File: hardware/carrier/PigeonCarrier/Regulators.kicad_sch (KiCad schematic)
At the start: 0 parts

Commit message: shortned readmes + start of power stuff
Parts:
- added C1: 100nF, PCM_JLCPCB:C_0402, symbol PCM_JLCPCB-Capacitors:0402,100nF,(2)
- added U2: LM74502DDFR, PigeonVision:Texas_DDF0008A_SOT-8_1.6x2.9mm_P0.65mm, symbol PigeonVision:LM74502DDFR
- added U3: INA226AIDGSR, PigeonVision:TI_DGS0010A_VSSOP-10_3x3mm_P0.5mm, symbol PigeonVision:INA226AIDGSR
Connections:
- new net VBAT_RAW: C1.1, U2.5 (VS)
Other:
- added sheet VBAT->5V_MAIN (batt_5V_main.kicad_sch)
- added sheet VBAT->5V_SDR (batt_5V_sdr.kicad_sch)
- note added: "Reverse Polarity Protection"
- note added: "UVLO:"

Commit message: carrier progress
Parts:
- added C2: 220nF, PCM_JLCPCB:C_0805, symbol PCM_JLCPCB-Capacitors:0805,220nF
- added C3: 100nF, PCM_JLCPCB:C_0402, symbol PCM_JLCPCB-Capacitors:0402,100nF,(2)
- added C8: 1uF, PCM_JLCPCB:C_0603, symbol PCM_JLCPCB-Capacitors:0603,1uF
- added C9: 220uF, JLCImport_Auto:EEEFK1V221P, symbol JLCImport_Auto:EEEFK1V221P
- added J4: PULL_PIN, symbol Connector_Generic:Conn_01x02
- added LED1, LED2, LED3: 0805G_Green, JLCImport_Auto:0805G_Green, symbol JLCImport_Auto:0805G_Green
- added Q1, Q2: CSD18540Q5B, Package_TO_SOT_SMD:TDSON-8-1, symbol Transistor_FET:CSD18540Q5B
- added R1: 7.5kΩ, PCM_JLCPCB:R_0402, symbol PCM_JLCPCB-Resistors:0402,7.5kΩ
- added R2, R20, R25: 1kΩ, PCM_JLCPCB:R_0402, symbol PCM_JLCPCB-Resistors:0402,1kΩ
- added R27: 560Ω, PCM_JLCPCB:R_0603, symbol PCM_JLCPCB-Resistors:0603,560Ω
- added R3: 51kΩ, PCM_JLCPCB:R_0402, symbol PCM_JLCPCB-Resistors:0402,51kΩ
- added R4: 4.7kΩ, PCM_JLCPCB:R_0402, symbol PCM_JLCPCB-Resistors:0402,4.7kΩ
- added R5, R7: 10, PCM_JLCPCB:R_0402, symbol Device:R
- added R6: 5mΩ, PigeonVision:Vishay_WSL2512_5mOhm_2W, symbol PigeonVision:WSL25125L000FEA18
- added TP1: VBAT_RAW, TestPoint:TestPoint_Pad_D2.0mm, symbol Connector:TestPoint
- added TP2: 5V_MAIN, TestPoint:TestPoint_Pad_D2.0mm, symbol Connector:TestPoint
- added TP3: 5V_RF, TestPoint:TestPoint_Pad_D2.0mm, symbol Connector:TestPoint
- added TP4: 4V_CAM, TestPoint:TestPoint_Pad_D2.0mm, symbol Connector:TestPoint
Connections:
- net VBAT_RAW: now also C2.1, Q1.5 (D), R1.1, R3.1, TP1.1
- net GND: now reaches U3.1 (A1)
- net GND: now also C1.2, U2.2 (GND), U3.2 (A0), U3.7 (GND), C3.2, C9.2, J4.2 (Pin_2), LED1.2 (K), LED2.2 (K), LED3.2 (K), R2.2, R4.2
- net at U3.10 (Vin+): now also C8.1, R5.2
- net SDA_0: now reaches U3.4 (SDA)
- net SCL_0: now reaches U3.5 (SCL)
- net +3V3: now reaches U3.6 (VS)
- net +3V3: now also C3.1
- net at U3.8 (Vbus): now also Q2.5 (D), R5.1, R6.1
- net at U3.9 (Vin-): now also C8.2, R7.2
- net PWR_EN: now reaches U2.1 (EN/UVLO)
- net PWR_EN: now also J4.1 (Pin_1), R1.2, R2.1
- net at U2.4 (VCAP): now also C2.2
- net at U2.6 (GATE): now also Q1.4 (G), Q2.4 (G)
- net at U2.7 (OV): now also R3.2, R4.1
- net at U2.8 (SRC): now also Q1.1 (S), Q1.2 (S), Q1.3 (S), Q2.1 (S), Q2.2 (S), Q2.3 (S)
- new net: LED2.1 (A), R25.2
- new net: LED1.1 (A), R20.2
- new net: LED3.1 (A), R27.2
- new net 4V_CAM: R27.1, TP4.1
- new net 5V_MAIN: R20.1, TP2.1
- new net 5V_RF: R25.1, TP3.1
- new net VBAT: C9.1, R6.2, R7.1
- no-connect marks 0 -> 2
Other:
- sheet VBAT->5V_SDR renamed VBAT->5V_RF
- added sheet 5V_MAIN -> Cam Regs (Camera_Regulators.kicad_sch)
- note added: "6 * 0.005 = 30mV"
- note added: "6^2 * 0.005 = 0.18W"
- note added: "ADDR: 1000000"
- note added: "Current Sensing"
- note added: "External switch: pin IN = closed / OFF Pin OUT = open / ON (UVLO still active) Connector / footprint TBD; no latching Shut down CM5 before reinserting pin"
- note added: "Fc = 8.0 kHz"
- note added: "Overvoltage: 14.81V"
- note added: "Pin Switch RBF Inhibit"
- note added: "Reverse Polarity, Overvoltage Protection"
- note added: "Shunt"
- note added: "UVLO: Off = 9.69V, Restart = 10.54V"
- note added: "~16.4A Measurement Limit"
- note added: "~2.1mA"
- note added: "~2.2mA"
- note removed: "Reverse Polarity Protection"
- note removed: "UVLO:"
- moved on the sheet: C1, U2, U3

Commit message: Update carrier schematics, parts library, and JLC rules
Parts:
- removed R27: 560Ω, PCM_JLCPCB:R_0603, symbol PCM_JLCPCB-Resistors:0603,560Ω
- removed R3: 51kΩ, PCM_JLCPCB:R_0402, symbol PCM_JLCPCB-Resistors:0402,51kΩ
- added R4: 56kΩ, PCM_JLCPCB:R_0402, symbol PCM_JLCPCB-Resistors:0402,56kΩ
- added R6: 220Ω, PCM_JLCPCB:R_0402, symbol PCM_JLCPCB-Resistors:0402,220Ω
- added TP4, TP5, TP6: GND, TestPoint:TestPoint_Pad_D2.0mm, symbol Connector:TestPoint
- TP2: renamed from TP4; value 4V_CAM -> 3V3_CAM
- renumbered C1 to C2, C2 to C3, C9 to C4, C8 to C5, C3 to C6, J4 to J6, LED3 to LED1, LED1 to LED2, LED2 to LED3, R7 to R10, R25 to R11, R1 to R2, R2 to R3, R4 to R5, R6 to R7, R20 to R8, R5 to R9, TP2 to TP3, TP3 to TP7, U2 to U1, U3 to U2
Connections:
- net GND: now also TP4.1, TP5.1, TP6.1
- net VBAT_RAW: now also R4.1
- net at R5.1, U1.7 (OV): now also R4.2
- net at LED1.1 (A): now also R6.2
- net +3V3 renamed 3V3_CM5
- net 4V_CAM renamed 3V3_CAM
- net 3V3_CAM: now also R6.1
- net SCL_0 renamed SENSOR_I2C_SCL
- net SDA_0 renamed SENSOR_I2C_SDA
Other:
- sheet 5V_MAIN -> Cam Regs renamed VBAT -> 3V3_CAM
- sheet VBAT -> 3V3_CAM ports: added none; removed 1V8_CAM_EN, 4V_CAM_EN
- sheet VBAT->5V_RF ports: added 5V_RF_EN; removed none
- note added: "External switch: pin IN = closed / OFF Pin OUT = open / ON"
- note added: "Overvoltage: 16.14V"
- note added: "To be placed near power TP for GND Springs"
- note removed: "External switch: pin IN = closed / OFF Pin OUT = open / ON (UVLO still active) Connector / footprint TBD; no latching Shut down CM5 before reinserting pin"
- note removed: "Overvoltage: 14.81V"
- note removed: "~2.1mA"
- moved on the sheet: LED1, LED2, LED3, R11, R8, TP2, TP3, TP7

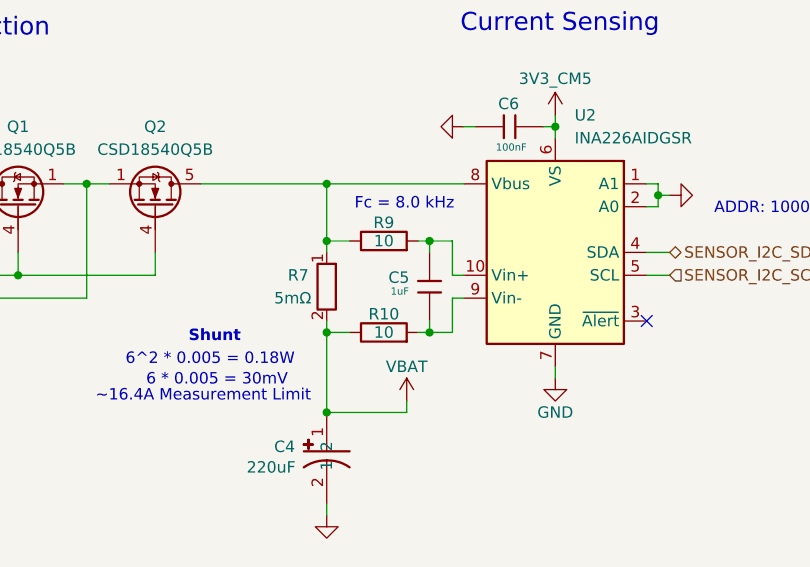
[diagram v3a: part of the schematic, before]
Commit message: Replace remaining 1 uF X5R capacitors with X7R
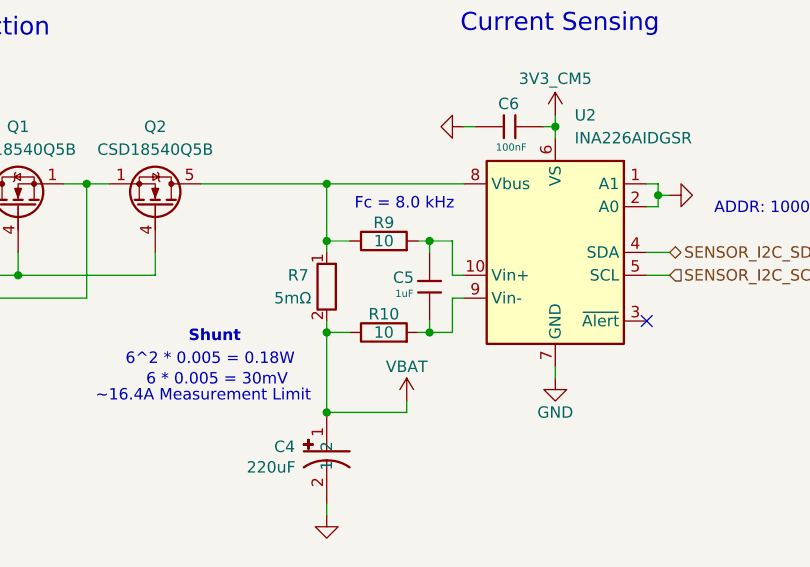
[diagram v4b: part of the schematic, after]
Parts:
- removed C5: 1uF, PCM_JLCPCB:C_0603, symbol PCM_JLCPCB-Capacitors:0603,1uF
- added C5: 1uF, PCM_JLCPCB:C_0805, symbol PCM_JLCPCB-Capacitors:0805,1uF
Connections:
- net at R9.2, U2.10 (Vin+): now also C5.1
- net at R10.2, U2.9 (Vin-): now also C5.2
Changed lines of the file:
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@@
+	)
+	(symbol
+		(lib_id "PCM_JLCPCB-Capacitors:0805,1uF")
+		(at 144.78 50.8 0)
+		(unit 1)
+		(body_style 1)
+		(exclude_from_sim no)
+		(in_bom yes)
+		(on_board yes)
+		(in_pos_files yes)
+		(dnp no)
+		(property "Reference" "C5"
+			(at 140.716 49.784 0)
+			(show_name no)
+			(do_not_autoplace no)
+			(effects
+				(font
+					(size 1.27 1.27)
+				)
+				(justify left)
+			)
+		)
+		(property "Value" "1uF"
+			(at 140.97 51.562 0)
+			(show_name no)
+			(do_not_autoplace no)
+			(effects
+				(font
+					(size 0.8 0.8)
+				)
+				(justify left)
+			)
+		)
+		(property "Footprint" "PCM_JLCPCB:C_0805"
+			(at 143.002 50.8 90)
+			(hide yes)
+			(show_name no)
+			(do_not_autoplace no)
+			(effects
+				(font
+					(size 1.27 1.27)
+				)
+			)
+		)
+		(property "Datasheet" "https://www.lcsc.com/datasheet/lcsc_datasheet_2304140030_Samsung-Electro-Mechanics-CL21B105KBFNNNE_C28323.pdf"
+			(at 144.78 50.8 0)
+			(hide yes)
+			(show_name no)
+			(do_not_autoplace no)
+			(effects
+				(font
+					(size 1.27 1.27)
+				)
+			)
+		)
+		(property "Description" "50V 1uF X7R ±10% 0805 Multilayer Ceramic Capacitors MLCC - SMD/SMT ROHS"
+			(at 144.78 50.8 0)
+			(hide yes)
+			(show_name no)
+			(do_not_autoplace no)
+			(effects
+				(font
+					(size 1.27 1.27)
+				)
+			)
+		)
+		(property "LCSC" "C28323"
+			(at 144.78 50.8 0)
+			(hide yes)
+			(show_name no)
+			(do_not_autoplace no)
+			(effects
+				(font
+					(size 1.27 1.27)
+				)
+			)
+		)
+		(property "Stock" "4334256"
+			(at 144.78 50.8 0)
+			(hide yes)
+			(show_name no)
+			(do_not_autoplace no)
+			(effects
+				(font
+					(size 1.27 1.27)
+				)
+			)
+		)
+		(property "Price" "0.012USD"
+			(at 144.78 50.8 0)
+			(hide yes)
+			(show_name no)
+			(do_not_autoplace no)
+			(effects
+				(font
+					(size 1.27 1.27)
+				)
+			)
+		)
+		(property "Process" "SMT"
+			(at 144.78 50.8 0)
+			(hide yes)
+			(show_name no)
+			(do_not_autoplace no)
+			(effects
+				(font
+					(size 1.27 1.27)
+				)
+			)
+		)
+		(property "Minimum Qty" "20"
+			(at 144.78 50.8 0)
+			(hide yes)
+			(show_name no)
+			(do_not_autoplace no)
+			(effects
+				(font
+					(size 1.27 1.27)
+				)
+			)
+		)
+		(property "Attrition Qty" "10"
+			(at 144.78 50.8 0)
+			(hide yes)
+			(show_name no)
+			(do_not_autoplace no)
+			(effects
+				(font
+					(size 1.27 1.27)
+				)
+			)
+		)
+		(property "Class" "Basic Component"
+			(at 144.78 50.8 0)
+			(hide yes)
+			(show_name no)
+			(do_not_autoplace no)
+			(effects
+				(font
+					(size 1.27 1.27)
+				)
+			)
+		)
+		(property "Category" "Capacitors,Multilayer Ceramic Capacitors MLCC - SMD/SMT"
+			(at 144.78 50.8 0)
+			(hide yes)
+			(show_name no)
+			(do_not_autoplace no)
+			(effects
+				(font
+					(size 1.27 1.27)
+				)
+			)
+		)
+		(property "Manufacturer" "Samsung Electro-Mechanics"
+			(at 144.78 50.8 0)
+			(hide yes)
+			(show_name no)
+			(do_not_autoplace no)
+			(effects
+				(font
+					(size 1.27 1.27)
+				)
+			)
+		)
+		(property "Part" "CL21B105KBFNNNE"
+			(at 144.78 50.8 0)
+			(hide yes)
+			(show_name no)
+			(do_not_autoplace no)
+			(effects
+				(font
+					(size 1.27 1.27)
+				)
+			)
+		)
+		(property "Voltage Rated" "50V"
+			(at 147.32 53.34 0)
+			(hide yes)
+			(show_name no)
+			(do_not_autoplace no)
+			(effects
+				(font
+					(size 0.8 0.8)
+				)
+				(justify left)
+			)
+		)
+		(property "Tolerance" "±10%"
+			(at 144.78 50.8 0)
+			(hide yes)
+			(show_name no)
+			(do_not_autoplace no)
+			(effects
+				(font
+					(size 1.27 1.27)
+				)
+			)
+		)
+		(property "Capacitance" "1uF"
+			(at 144.78 50.8 0)
+			(hide yes)
+			(show_name no)
+			(do_not_autoplace no)
+			(effects
+				(font
+					(size 1.27 1.27)
+				)
+			)
+		)
+		(property "Temperature Coefficient" "X7R"
+			(at 144.78 50.8 0)
+			(hide yes)
+			(show_name no)
+			(do_not_autoplace no)
+			(effects
+				(font
+					(size 1.27 1.27)
+				)
+			)
+		)
+		(pin "1"
+		)
+		(pin "2"
+		)
+		(instances
+			(project "PigeonCarrier"
+				(path "/6c8da0f4-34cf-43b9-a25b-857048b8016b/7986dfff-dfed-4d72-b8d7-0f8819bc467b"
+					(reference "C5")
+					(unit 1)
+				)
+			)
+		)
 	)
 	(symbol
@@
 					(unit 1)
 				)
-			)
-		)
-	)
-	(symbol
-		(lib_id "PCM_JLCPCB-Capacitors:0603,1uF")
-		(at 144.78 50.8 0)
-		(unit 1)
-		(body_style 1)
-		(exclude_from_sim no)
-		(in_bom yes)
-		(on_board yes)
-		(in_pos_files yes)
-		(dnp no)
-		(property "Reference" "C5"
-			(at 140.208 49.784 0)
-			(show_name no)
-			(do_not_autoplace no)
-			(effects
-				(font
-					(size 1.27 1.27)
-				)
-				(justify left)
-			)
-		)
-		(property "Value" "1uF"
-			(at 140.462 51.308 0)
-			(show_name no)
-			(do_not_autoplace no)
-			(effects
-				(font
-					(size 0.8 0.8)
-				)
-				(justify left)
-			)
-		)
-		(property "Footprint" "PCM_JLCPCB:C_0603"
-			(at 143.002 50.8 90)
-			(hide yes)
-			(show_name no)
-			(do_not_autoplace no)
-			(effects
-				(font
-					(size 1.27 1.27)
-				)
-			)
-		)
-		(property "Datasheet" "https://www.lcsc.com/datasheet/lcsc_datasheet_2304140030_Samsung-Electro-Mechanics-CL10A105KB8NNNC_C15849.pdf"
-			(at 144.78 50.8 0)
-			(hide yes)
-			(show_name no)
-			(do_not_autoplace no)
-			(effects
-				(font
-					(size 1.27 1.27)
-				)
-			)
-		)
-		(property "Description" "50V 1uF X5R ±10% 0603 Multilayer Ceramic Capacitors MLCC - SMD/SMT ROHS"
-			(at 144.78 50.8 0)
-			(hide yes)
-			(show_name no)
-			(do_not_autoplace no)
-			(effects
-				(font
-					(size 1.27 1.27)
-				)
-			)
-		)
-		(property "LCSC" "C15849"
-			(at 144.78 50.8 0)
-			(hide yes)
-			(show_name no)
-			(do_not_autoplace no)
-			(effects
-				(font
-					(size 1.27 1.27)
-				)
-			)
-		)
-		(property "Stock" "11535980"
-			(at 144.78 50.8 0)
-			(hide yes)
-			(show_name no)
-			(do_not_autoplace no)
-			(effects
-				(font
-					(size 1.27 1.27)
-				)
-			)
-		)
-		(property "Price" "0.008USD"
-			(at 144.78 50.8 0)
-			(hide yes)
-			(show_name no)
-			(do_not_autoplace no)
-			(effects
-				(font
-					(size 1.27 1.27)
-				)
-			)
-		)
-		(property "Process" "SMT"
-			(at 144.78 50.8 0)
-			(hide yes)
-			(show_name no)
-			(do_not_autoplace no)
-			(effects
-				(font
-					(size 1.27 1.27)
-				)
-			)
-		)
-		(property "Minimum Qty" "20"
-			(at 144.78 50.8 0)
-			(hide yes)
-			(show_name no)
-			(do_not_autoplace no)
-			(effects
-				(font
-					(size 1.27 1.27)
-				)
-			)
-		)
-		(property "Attrition Qty" "10"
-			(at 144.78 50.8 0)
-			(hide yes)
-			(show_name no)
-			(do_not_autoplace no)
-			(effects
-				(font
-					(size 1.27 1.27)
-				)
-			)
-		)
-		(property "Class" "Basic Component"
-			(at 144.78 50.8 0)
-			(hide yes)
-			(show_name no)
-			(do_not_autoplace no)
-			(effects
-				(font
-					(size 1.27 1.27)
-				)
-			)
-		)
-		(property "Category" "Capacitors,Multilayer Ceramic Capacitors MLCC - SMD/SMT"
-			(at 144.78 50.8 0)
-			(hide yes)
-			(show_name no)
-			(do_not_autoplace no)
-			(effects
-				(font
-					(size 1.27 1.27)
-				)
-			)
-		)
-		(property "Manufacturer" "Samsung Electro-Mechanics"
-			(at 144.78 50.8 0)
-			(hide yes)
-			(show_name no)
-			(do_not_autoplace no)
-			(effects
-				(font
-					(size 1.27 1.27)
-				)
-			)
-		)
-		(property "Part" "CL10A105KB8NNNC"
-			(at 144.78 50.8 0)
-			(hide yes)
-			(show_name no)
-			(do_not_autoplace no)
-			(effects
-				(font
-					(size 1.27 1.27)
-				)
-			)
-		)
-		(property "Voltage Rated" "50V"
-			(at 147.32 53.34 0)
-			(hide yes)
-			(show_name no)
-			(do_not_autoplace no)
-			(effects
-				(font
-					(size 0.8 0.8)
-				)
-				(justify left)
-			)
-		)
-		(property "Tolerance" "±10%"
-			(at 144.78 50.8 0)
-			(hide yes)
-			(show_name no)
-			(do_not_autoplace no)
-			(effects
-				(font
-					(size 1.27 1.27)
-				)
-			)
-		)
-		(property "Capacitance" "1uF"
-			(at 144.78 50.8 0)
-			(hide yes)
-			(show_name no)
-			(do_not_autoplace no)
-			(effects
-				(font
-					(size 1.27 1.27)
-				)
-			)
-		)
-		(property "Temperature Coefficient" "X5R"
-			(at 144.78 50.8 0)
-			(hide yes)
-			(show_name no)
-			(do_not_autoplace no)
-			(effects
-				(font
-					(size 1.27 1.27)
-				)
-			)
-		)
-		(pin "2"
-		)
-		(pin "1"
-		)
-		(instances
-			(project "PigeonCarrier"
-				(path "/6c8da0f4-34cf-43b9-a25b-857048b8016b/7986dfff-dfed-4d72-b8d7-0f8819bc467b"
-					(reference "C5")
-					(unit 1)
-				)

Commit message: finished rough layout
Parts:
- C2, C6: MPN (none) -> CL05B104KB54PNC
- C3: MPN (none) -> CL21B224KBFNNNE
- C4: footprint JLCImport_Auto:EEEFK1V221P -> PigeonVision:Panasonic_EEE-FK1V221P_CaseF_8x10.2mm; MPN (none) -> EEEFK1V221P
- C5: MPN (none) -> CL21B105KBFNNNE
- J6: footprint (none) -> Connector_AMASS:AMASS_XT30PW-M_1x02_P2.50mm_Horizontal; MPN (none) -> XT30PW-M; Manufacturer (none) -> AMASS
- LED1, LED2, LED3: MPN (none) -> KT-0805G
- Q1, Q2: footprint Package_TO_SOT_SMD:TDSON-8-1 -> PigeonVision:TI_CSD18540Q5B_Q5B; MPN (none) -> CSD18540Q5B; Manufacturer (none) -> Texas Instruments
- R10, R9: value 10 -> 10Ω; symbol Device:R -> PCM_JLCPCB-Resistors:0402,10Ω; Attrition Qty (none) -> 10; Category (none) -> Resistors,Chip Resistor - Surface Mount; Class (none) -> Basic Component; MPN (none) -> 0402WGF100JTCE; Minimum Qty (none) -> 20; Operating Temperature Range (none) -> -55°C~+155°C; Overload Voltage (Max) (none) -> 50V; Part (none) -> 0402WGF100JTCE; Power(Watts) (none) -> 62.5mW; Price (none) -> 0.004USD; Process (none) -> SMT; Resistance (none) -> 10Ω; Stock (none) -> 4873481; Temperature Coefficient (none) -> ±200ppm/°C; Tolerance (none) -> ±1%; Type (none) -> Thick Film Resistors
- R11, R3, R8: MPN (none) -> 0402WGF1001TCE
- R2: MPN (none) -> 0402WGF7501TCE
- R4: MPN (none) -> 0402WGF5602TCE
- R5: MPN (none) -> 0402WGF4701TCE
- R6: MPN (none) -> 0402WGF2200TCE
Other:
- note added: "Pin IN: closed / OFF Pin OUT: open / ON"
- note added: "Pin Switch"
- note removed: "External switch: pin IN = closed / OFF Pin OUT = open / ON"
- note removed: "Pin Switch RBF Inhibit"
- moved on the sheet: J6

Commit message: Update carrier placement and vertical connector libraries
Save the latest component placements and mechanical mounting changes. Include the vertical XT60/XT30 and camera connector symbols, footprints, redistributable CAD, licenses and documentation. Keep local-only vendor models ignored.

Validation: ERC has zero findings. Native KiCad loading and netlist comparison confirm all 152 schematic components and 681 numbered pads agree. Full DRC could not complete because the KiCad CLI aborted in this environment.
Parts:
- J6: footprint Connector_AMASS:AMASS_XT30PW-M_1x02_P2.50mm_Horizontal -> PigeonVision:AMASS_XT30UPB-M_1x02_P5.00mm_Vertical_2025; symbol Connector_Generic:Conn_01x02 -> PigeonVision:AMASS_XT30UPB_M_G_Y; JLC Part # (none) -> C428721; LCSC Part # (none) -> C428721; MPN XT30PW-M -> XT30UPB-M.G.Y; Sourcing note (none) -> JLC short MPN XT30UPB-M C428721;manufacturer2025V1 full yel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
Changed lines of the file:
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@@
 	)
 	(symbol
-		(lib_id "Connector_Generic:Conn_01x02")
+		(lib_id "PigeonVision:AMASS_XT30UPB_M_G_Y")
 		(at 44.45 88.9 0)
 		(mirror y)
@@
 			)
 		)
-		(property "Footprint" "Connector_AMASS:AMASS_XT30PW-M_1x02_P2.50mm_Horizontal"
+		(property "Footprint" "PigeonVision:AMASS_XT30UPB-M_1x02_P5.00mm_Vertical_2025"
 			(at 44.45 88.9 0)
 			(hide yes)
@@
 			)
 		)
-		(property "Datasheet" "https://www.tme.eu/Document/6eb2005a51a52592b3f19e8a450c54c8/XT30PW-M.pdf"
+		(property "Datasheet" "https://www.china-amass.net/uploads/XT30UPB-FM.rar"
 			(at 44.45 88.9 0)
 			(hide yes)
@@
 			)
 		)
-		(property "Description" "External COM-NO contact: pin inserted/lever pressed = closed/OFF; pin removed/lever released = open/ON. J6.1 directly inhibits EN/UVLO, J6.2 is GND."
+		(property "Description" "External COM-NO contact: pin inserted/lever pressed = closed/OFF; pin removed/lever released = open/ON. J6.1 directly inhibits EN/UVLO, J6.2 is GND. Vertical AMASS XT30UPB-M.G.Y; pin 1 keyed/minus-marked, pin 2 flat/plus-marked."
 			(at 44.45 88.9 0)
 			(hide yes)
@@
 			)
 		)
-		(property "MPN" "XT30PW-M"
+		(property "MPN" "XT30UPB-M.G.Y"
 			(at 36.83 87.63 0)
 			(hide yes)
@@
 			)
 		)
-	)
+	(property "LCSC Part #" "C428721" (at 44.45 88.9 0) (hide yes) (effects (font (size 1.27 1.27))))
+	(property "JLC Part #" "C428721" (at 44.45 88.9 0) (hide yes) (effects (font (size 1.27 1.27))))
+	(property "Sourcing note" "JLC short MPN XT30UPB-M C428721;manufacturer2025V1 full yellow SKU XT30UPB-M.G.Y. Stock quantity not exposed in public page." (at 44.45 88.9 0) (hide yes) (effects (font (size 1.27 1.27))))
+)
 	(sheet
 		(at 78.105 144.78)
